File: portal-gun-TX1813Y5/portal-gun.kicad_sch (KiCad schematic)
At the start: 8 parts, among them J1 SAO, SW1 SW_Push

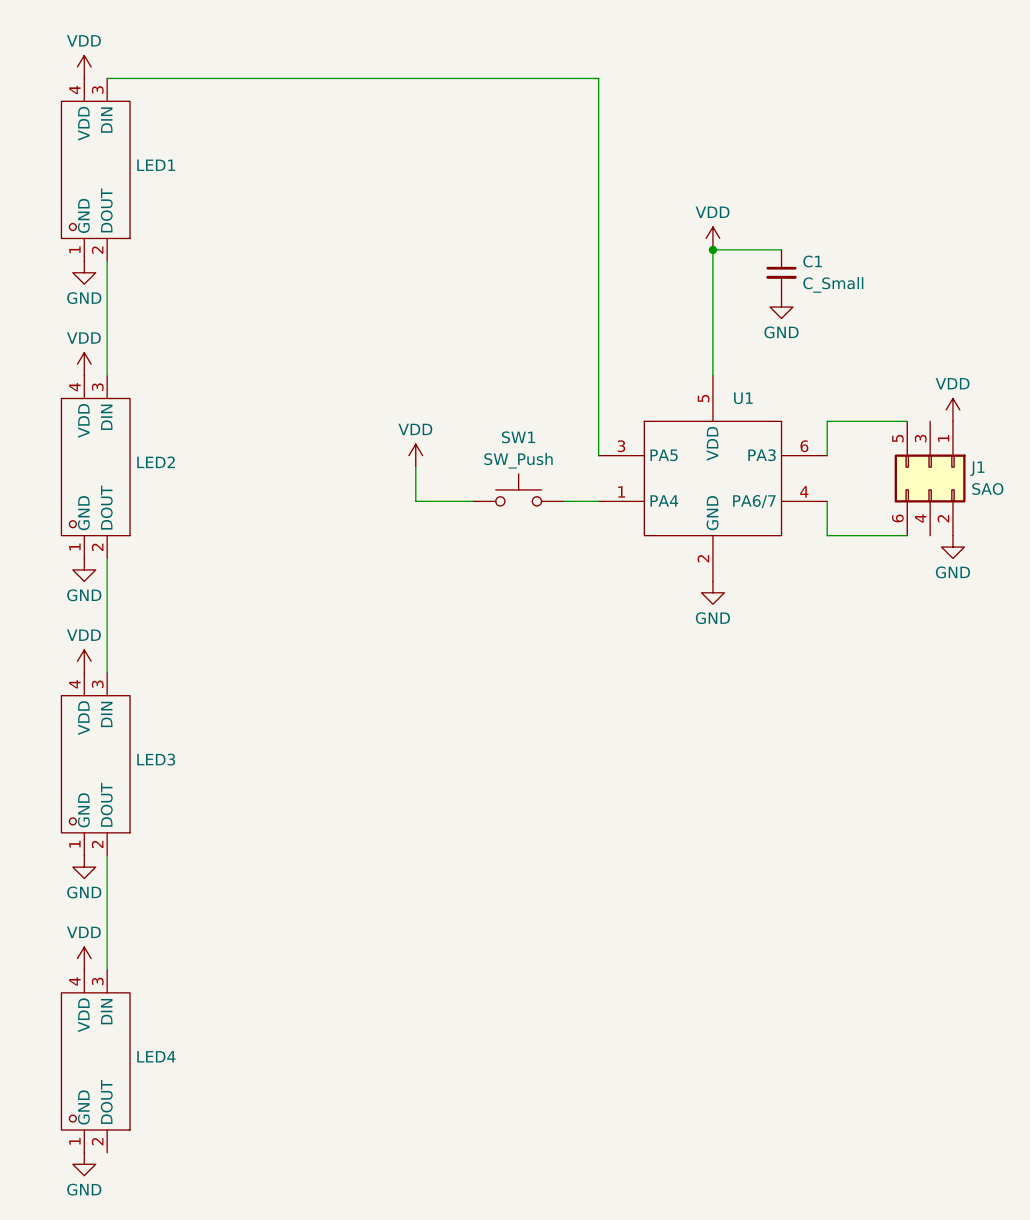
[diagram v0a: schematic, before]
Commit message: change over to different LED and fix design
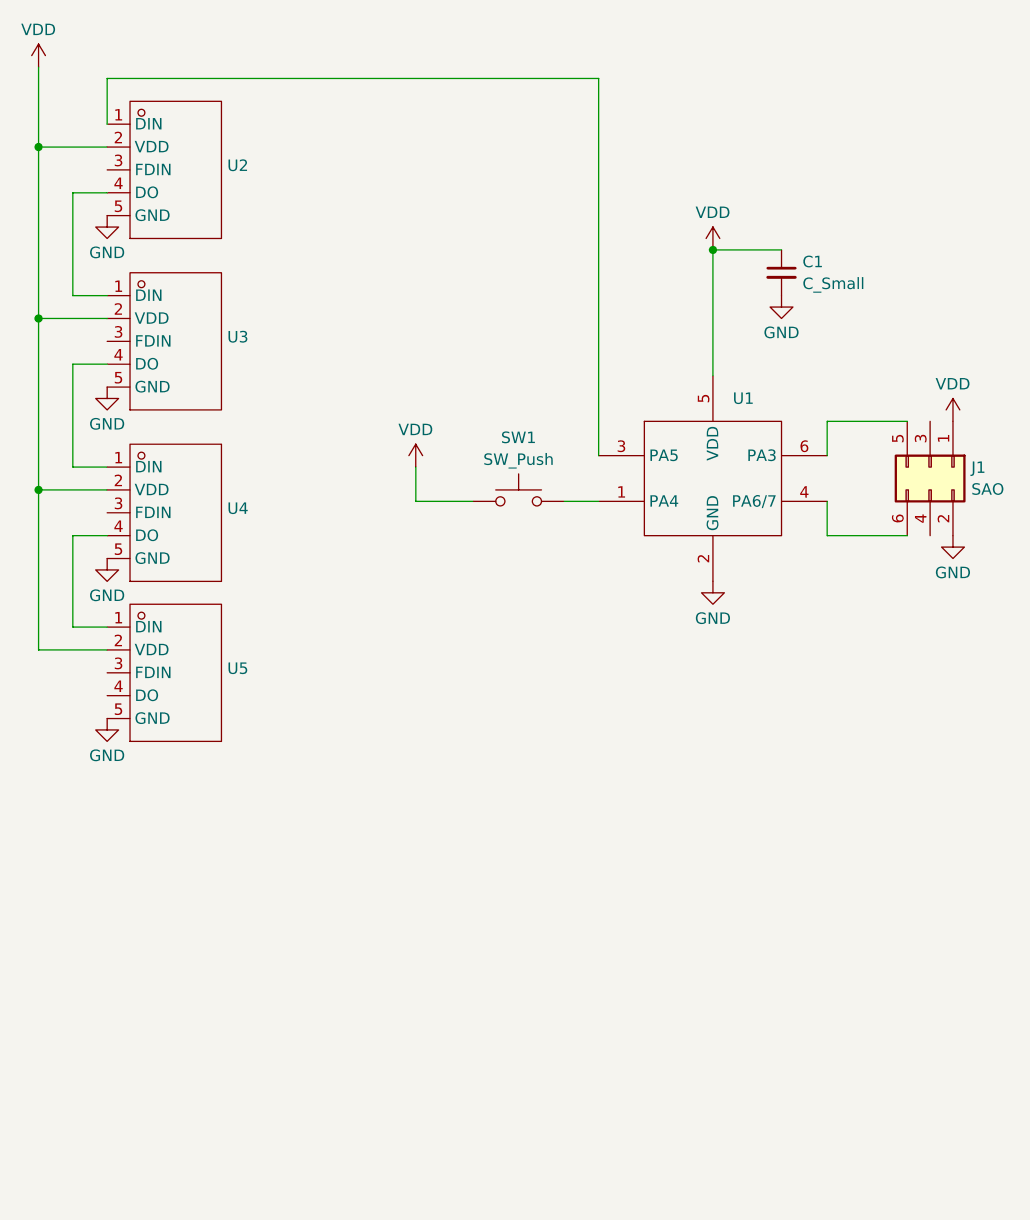
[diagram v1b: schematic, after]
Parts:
- removed LED1, LED2, LED3, LED4: ~, LED_SMD:LED-SMD_4P_SK6812D-EC3210R, symbol LED:SK6812D-EC3210R
- added U2, U3, U4, U5: ~, LED_SMD:LED-SMD_5P-L3.2-W1.4_TX1813Y5, symbol LED:TX1813Y5
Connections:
- net GND: now also U2.5 (GND), U3.5 (GND), U4.5 (GND), U5.5 (GND)
- net VDD: now also U2.2 (VDD), U3.2 (VDD), U4.2 (VDD), U5.2 (VDD)
- net at U1.3 (PA5): now also U2.1 (DIN)
- new net: U4.4 (DO), U5.1 (DIN)
- new net: U2.4 (DO), U3.1 (DIN)
- new net: U3.4 (DO), U4.1 (DIN)
